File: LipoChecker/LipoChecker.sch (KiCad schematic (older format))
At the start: 47 parts, among them J1 Battery, U1 LM358, U2 LM358, U3 LM358, U4 LM358, U5 LM358, U6 LM358, U7 MCP3208

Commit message: シミュレーションをついか
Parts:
- removed unit 1 of U5
- removed unit 2 of U5
- removed unit 1 of U6
- added U8, U9: LM358, symbol Amplifier_Operational:LM358
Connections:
- net at R16.1, R25.2: now also U4.6 (-); no longer U4.5 (+)
- net at R17.1, R18.2: now also U4.5 (+); no longer U4.6 (-)
- net at R29.1, U7.4 (CH3): now also U8.1
- net at R20.1, R22.2: now also U8.3 (+)
- net at R19.1, R29.2: now also U8.2 (-)
- net at R23.1, R31.2: now also U8.6 (-)
- net at R24.1, R26.2: now also U8.5 (+)
- net at R31.1, U7.5 (CH4): now also U8.7
- net at R32.1, U7.6 (CH5): now also U9.1
- net at R28.1, R30.2: now also U9.3 (+)
- net at R27.1, R32.2: now also U9.2 (-)
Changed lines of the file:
@@
 EESchema Schematic File Version 4
+LIBS:LipoChecker-cache
 EELAYER 26 0
 EELAYER END
@@
 $EndComp
 $Comp
-L Amplifier_Operational:LM358 U4
-U 2 1 5DF9A5F7
-P 5000 2800
-F 0 "U4" H 5000 3167 50  0000 C CNN
-F 1 "LM358" H 5000 3076 50  0000 C CNN
-F 2 "" H 5000 2800 50  0001 C CNN
-F 3 "http://www.ti.com/lit/ds/symlink/lm2904-n.pdf" H 5000 2800 50  0001 C CNN
-	2    5000 2800
-	1    0    0    -1
-$EndComp
-$Comp
 L Device:R_Small R16
 U 1 1 5DF9A5FD
@@
 	3850 2900 4325 2900
 $Comp
-L Amplifier_Operational:LM358 U5
-U 1 1 5DF9FCA8
-P 5200 3725
-F 0 "U5" H 5200 4092 50  0000 C CNN
-F 1 "LM358" H 5200 4001 50  0000 C CNN
-F 2 "" H 5200 3725 50  0001 C CNN
-F 3 "http://www.ti.com/lit/ds/symlink/lm2904-n.pdf" H 5200 3725 50  0001 C CNN
-	1    5200 3725
-	1    0    0    -1
-$EndComp
-$Comp
 L Device:R_Small R19
 U 1 1 5DF9FCAF
@@
 	3850 3825 4525 3825
 $Comp
-L Amplifier_Operational:LM358 U5
-U 2 1 5DFA6D6E
-P 5400 4650
-F 0 "U5" H 5400 5017 50  0000 C CNN
-F 1 "LM358" H 5400 4926 50  0000 C CNN
-F 2 "" H 5400 4650 50  0001 C CNN
-F 3 "http://www.ti.com/lit/ds/symlink/lm2904-n.pdf" H 5400 4650 50  0001 C CNN
-	2    5400 4650
-	1    0    0    -1
-$EndComp
-$Comp
 L Device:R_Small R23
 U 1 1 5DFA6D75
@@
 	3850 4750 4725 4750
 $Comp
-L Amplifier_Operational:LM358 U6
-U 1 1 5DFB0700
-P 5625 5575
-F 0 "U6" H 5625 5942 50  0000 C CNN
-F 1 "LM358" H 5625 5851 50  0000 C CNN
-F 2 "" H 5625 5575 50  0001 C CNN
-F 3 "http://www.ti.com/lit/ds/symlink/lm2904-n.pdf" H 5625 5575 50  0001 C CNN
-	1    5625 5575
-	1    0    0    -1
-$EndComp
-$Comp
 L Device:R_Small R27
 U 1 1 5DFB0707
@@
 	3850 5675 4950 5675
 Connection ~ 5050 1875
-Connection ~ 5300 2800
 Wire Wire Line
 	5925 5575 6300 5575
@@
 Wire Wire Line
 	8975 2675 8975 2950
+$Comp
+L Amplifier_Operational:LM358 U4
+U 2 1 5DF70A70
+P 5000 2800
+F 0 "U4" H 5000 2433 50  0000 C CNN
+F 1 "LM358" H 5000 2524 50  0000 C CNN
+F 2 "" H 5000 2800 50  0001 C CNN
+F 3 "http://www.ti.com/lit/ds/symlink/lm2904-n.pdf" H 5000 2800 50  0001 C CNN
+	2    5000 2800
+	1    0    0    1
+$EndComp
+Connection ~ 5300 2800
+$Comp
+L Amplifier_Operational:LM358 U8
+U 1 1 5DF71163
+P 5200 3725
+F 0 "U8" H 5200 3358 50  0000 C CNN
+F 1 "LM358" H 5200 3449 50  0000 C CNN
+F 2 "" H 5200 3725 50  0001 C CNN
+F 3 "http://www.ti.com/lit/ds/symlink/lm2904-n.pdf" H 5200 3725 50  0001 C CNN
+	1    5200 3725
+	1    0    0    1
+$EndComp
+Connection ~ 5500 3725
+$Comp
+L Amplifier_Operational:LM358 U8
+U 2 1 5DF71211
+P 5400 4650
+F 0 "U8" H 5400 4283 50  0000 C CNN
+F 1 "LM358" H 5400 4374 50  0000 C CNN
+F 2 "" H 5400 4650 50  0001 C CNN
+F 3 "http://www.ti.com/lit/ds/symlink/lm2904-n.pdf" H 5400 4650 50  0001 C CNN
+	2    5400 4650
+	1    0    0    1
+$EndComp
+Connection ~ 5700 4650
+$Comp
+L Amplifier_Operational:LM358 U9
+U 1 1 5DF712BF
+P 5625 5575
+F 0 "U9" H 5625 5208 50  0000 C CNN
+F 1 "LM358" H 5625 5299 50  0000 C CNN
+F 2 "" H 5625 5575 50  0001 C CNN
+F 3 "http://www.ti.com/lit/ds/symlink/lm2904-n.pdf" H 5625 5575 50  0001 C CNN
+	1    5625 5575
+	1    0    0    1
+$EndComp
+Connection ~ 5925 5575
 $EndSCHEMATC

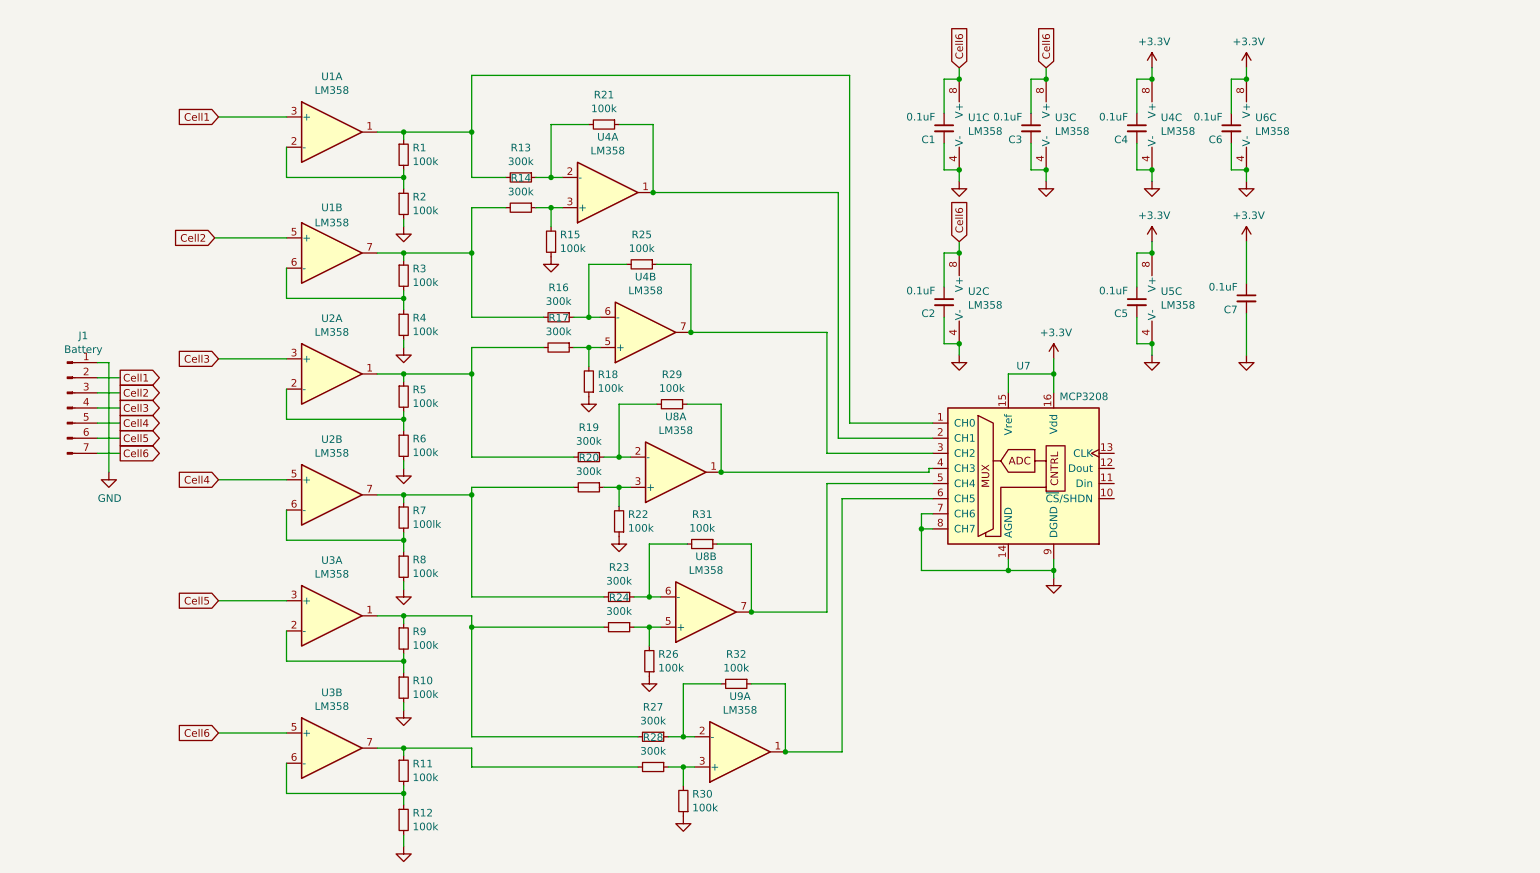
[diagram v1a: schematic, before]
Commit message: 電源まわりを変更
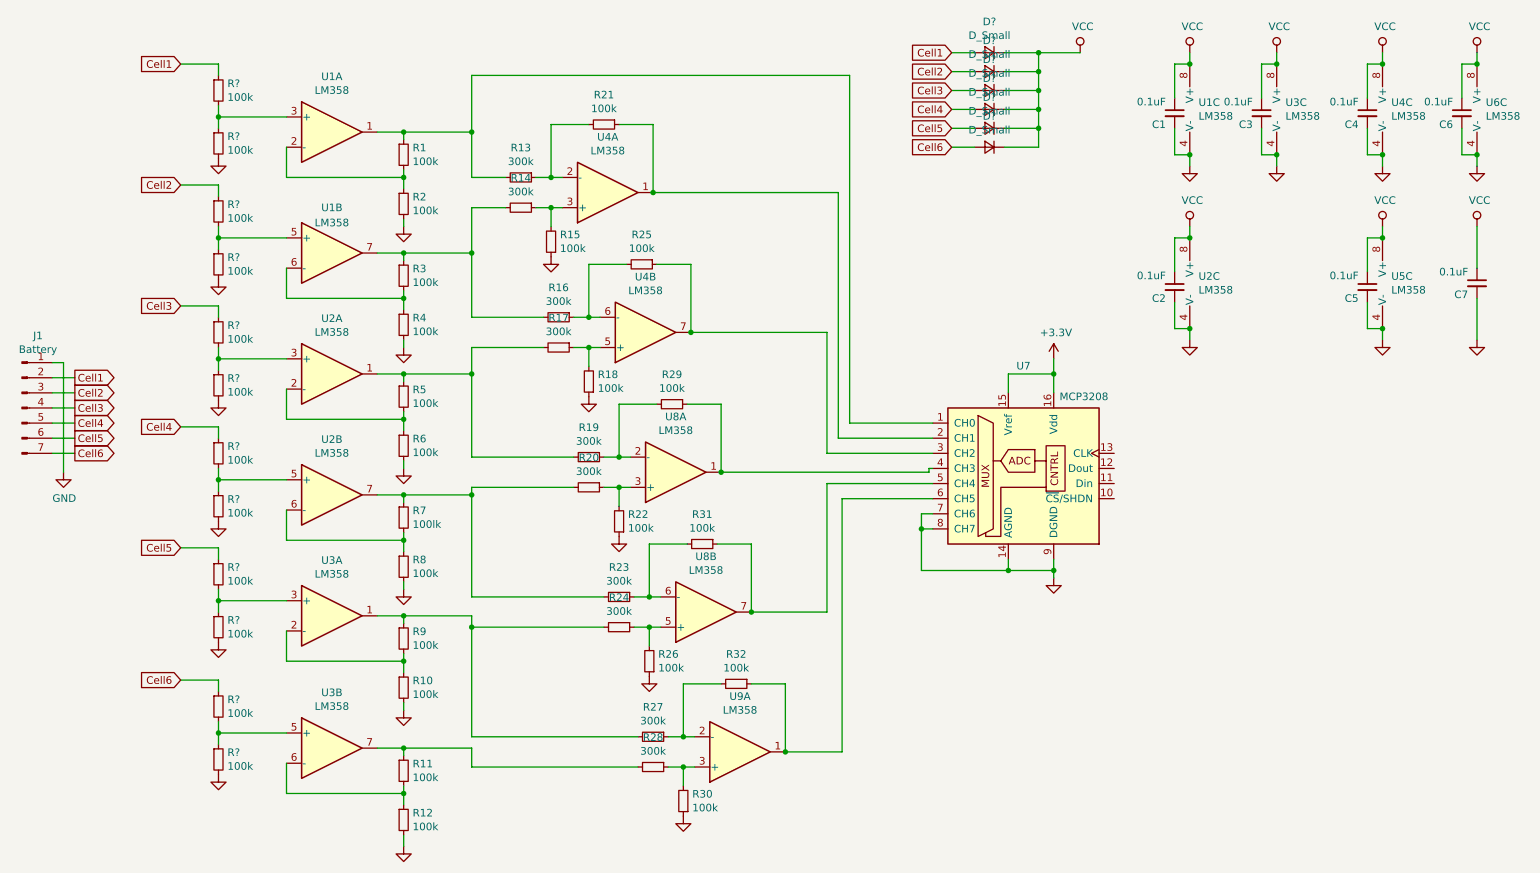
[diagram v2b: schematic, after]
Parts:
- added D? (x6): D_Small, symbol Device:D_Small
- added R? (x12): 100k, symbol Device:R_Small
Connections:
- net +3V3: no longer C4.1, C5.1, C6.1, C7.1, U4.8 (V+), U5.8 (V+), U6.8 (V+)
- net Cell1: now also D?.2 (A), R?.1; no longer U1.3 (+)
- net Cell2: now also D?.2 (A), R?.1; no longer U1.5 (+)
- net Cell3: now also D?.2 (A), R?.1; no longer U2.3 (+)
- net Cell4: now also D?.2 (A), R?.1; no longer U2.5 (+)
- net Cell5: now also D?.2 (A), R?.1; no longer U3.3 (+)
- net Cell6: now also D?.2 (A), R?.1; no longer C1.1, C2.1, C3.1, U1.8 (V+), U2.8 (V+), U3.5 (+), U3.8 (V+)
- net GND: now also R?.2, R?.2, R?.2, R?.2, R?.2, R?.2
- new net: R?.1, R?.2, U3.5 (+)
- new net: R?.1, R?.2, U3.3 (+)
- new net: R?.1, R?.2, U2.5 (+)
- new net: R?.1, R?.2, U2.3 (+)
- new net: R?.1, R?.2, U1.5 (+)
- new net: R?.1, R?.2, U1.3 (+)
- new net VCC: C1.1, C2.1, C3.1, C4.1, C5.1, C6.1, C7.1, D?.1 (K), D?.1 (K), D?.1 (K), D?.1 (K), D?.1 (K), D?.1 (K), U1.8 (V+), U2.8 (V+), U3.8 (V+), U4.8 (V+), U5.8 (V+), U6.8 (V+)
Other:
- moved on the sheet: C1, C2, C3, C4, C5, C6, C7, J1, U1C, U2C, U3C, U4C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
